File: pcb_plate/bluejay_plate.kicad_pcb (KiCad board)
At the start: 2 copper layers, 149.7 x 142.4 mm, 33 parts

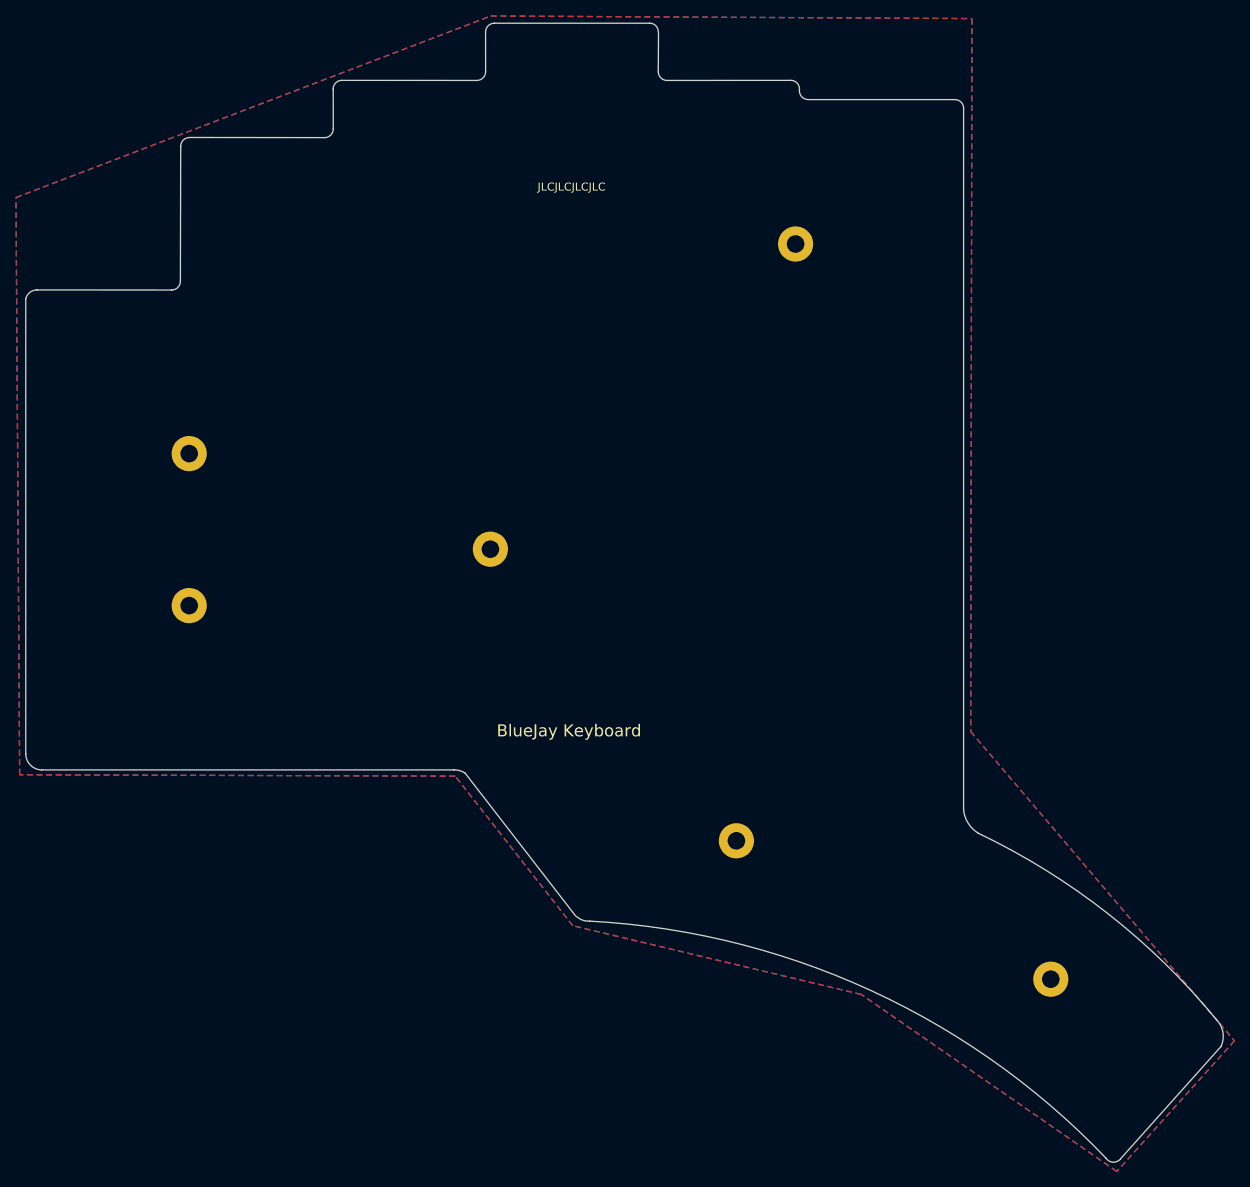
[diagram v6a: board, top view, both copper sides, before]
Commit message: Update placement of some components and size of drill holes
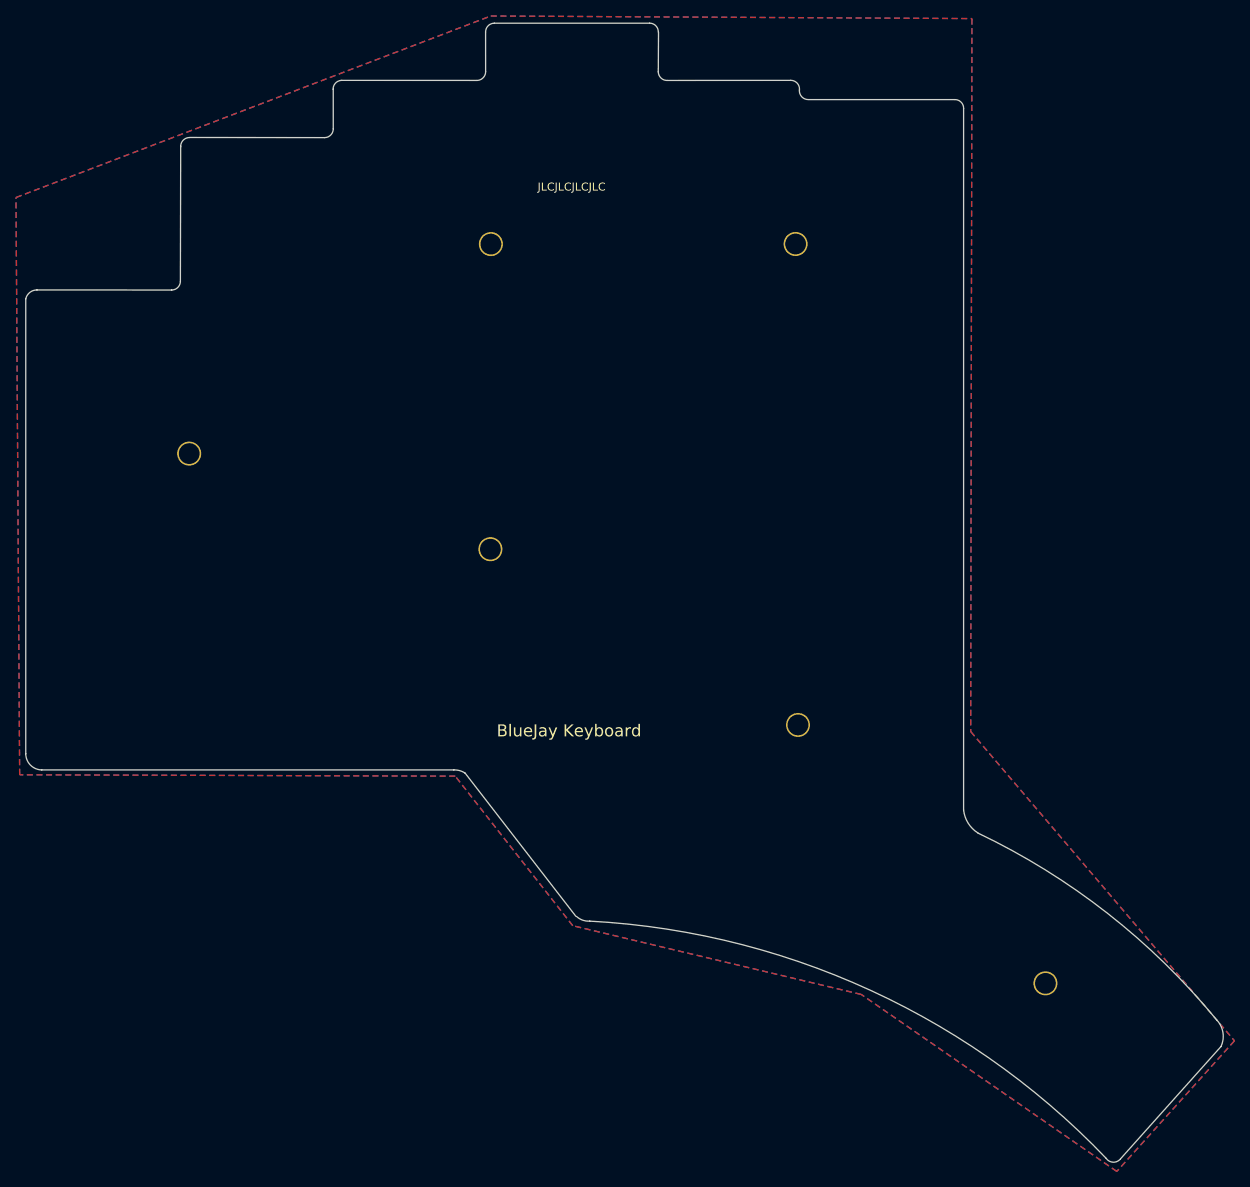
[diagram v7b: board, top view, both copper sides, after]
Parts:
- H3: footprint MountingHole:MountingHole_2.2mm_M2_Pad -> BlueJay footprints:MountingHole_2.2mm_M2_Pad
- H4, H5, H6, H7, H8: footprint MountingHole:MountingHole_2.2mm_M2_Pad -> BlueJay footprints:Drill hole
- moved H7 83.8 mm to (-66.8, -2.40)
- moved H3 60.1 mm to (9.30, 31.5)
- moved H5 54.0 mm to (9.00, -28.6)
- moved H4 45.9 mm to (-29.1, -28.6)
- moved H6 38.3 mm to (-29.1, 9.55)
- moved H8 0.85 mm to (40.2, 63.8)
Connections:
- H3 pad 1: GND -> (no net)
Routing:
- added copper zone on B.Cu, net (none)
- added copper zone on F.Cu, net (none)
- removed copper zone on B.Cu, net GND
- removed copper zone on F.Cu, net GND

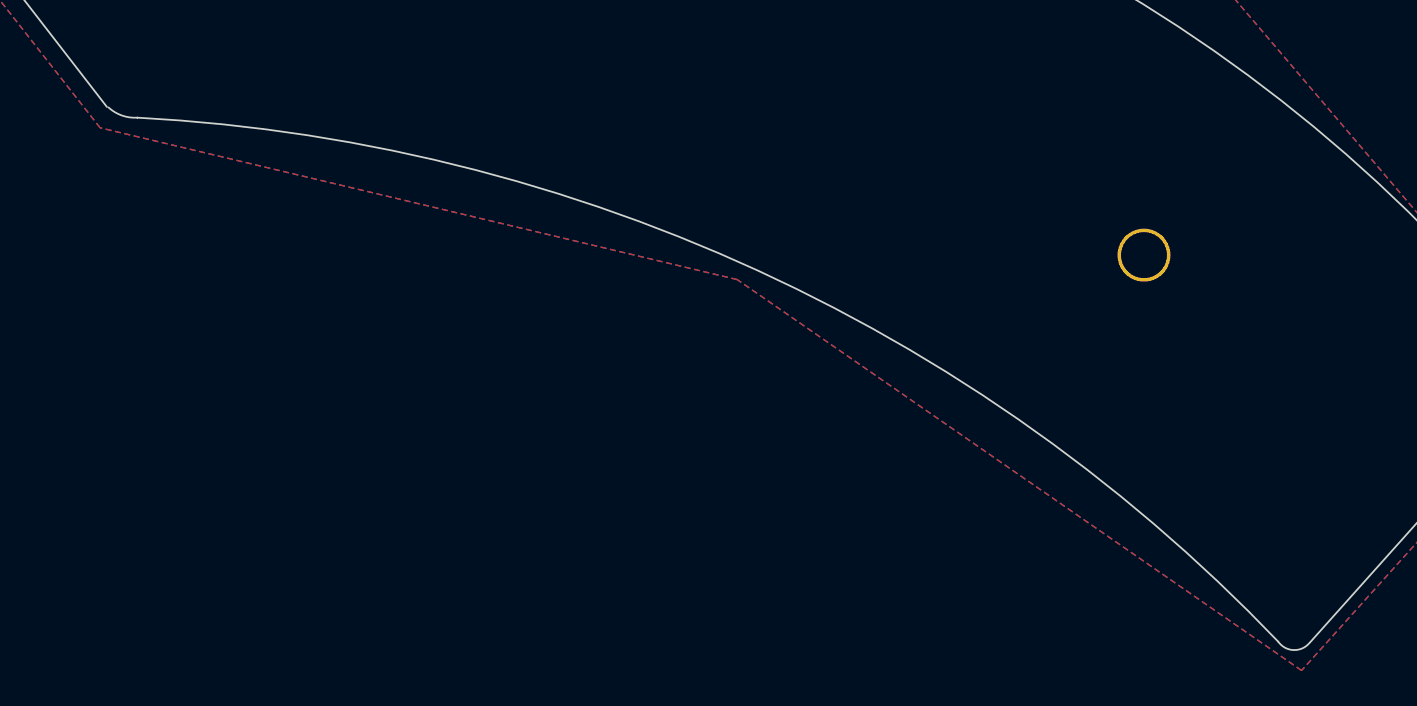
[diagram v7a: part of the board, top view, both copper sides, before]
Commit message: Fine tune edge cut
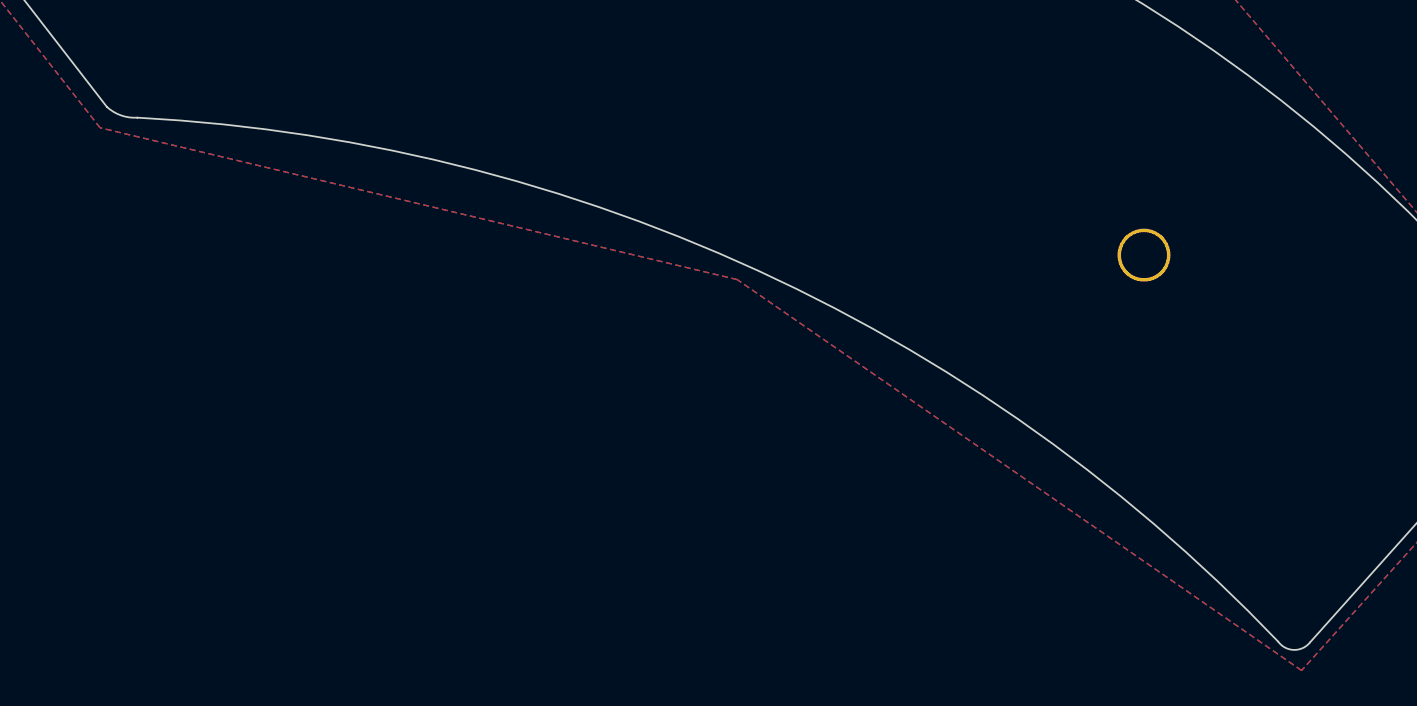
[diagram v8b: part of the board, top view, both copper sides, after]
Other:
- outline, holes or cut-outs redrawn
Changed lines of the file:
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@@
   (gr_line (start -9.26 -56.2) (end -28.66 -56.2) (layer "Edge.Cuts") (width 0.1))
   (gr_line (start -66.771552 -41.916351) (end -49.88133 -41.897097) (layer "Edge.Cuts") (width 0.1))
-  (gr_arc (start -16.74 56.04) (mid -17.619397 55.917949) (end -18.38 55.46) (layer "Edge.Cuts") (width 0.1))
+  (gr_arc (start -16.74 56.04) (mid -17.667469 55.912166) (end -18.47 55.43) (layer "Edge.Cuts") (width 0.1))
   (gr_line (start -47.736441 -49.055605) (end -30.836441 -49.046351) (layer "Edge.Cuts") (width 0.1))
   (gr_line (start 9.483077 -47.945267) (end 9.475373 -47.744734) (layer "Edge.Cuts") (width 0.1))
@@
   (gr_arc (start 31.782503 45.016513) (mid 30.564308 43.786562) (end 30 42.15) (layer "Edge.Cuts") (width 0.1))
   (gr_arc (start -29.751552 -55.085605) (mid -29.436575 -55.86887) (end -28.66 -56.2) (layer "Edge.Cuts") (width 0.1))
-  (gr_arc (start 49.59 85.78) (mid 48.690274 86.173968) (end 47.83 85.7) (layer "Edge.Cuts") (width 0.1))
+  (gr_arc (start 49.62 85.75) (mid 48.712671 86.166365) (end 47.83 85.7) (layer "Edge.Cuts") (width 0.1))
   (gr_arc (start -67.861552 -40.795605) (mid -67.546441 -41.576351) (end -66.771552 -41.905605) (layer "Edge.Cuts") (width 0.1))
   (gr_arc (start 8.393077 -49.055267) (mid 9.173279 -48.731231) (end 9.483077 -47.945267) (layer "Edge.Cuts") (width 0.1))
